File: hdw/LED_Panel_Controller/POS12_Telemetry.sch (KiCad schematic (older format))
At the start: 7 parts

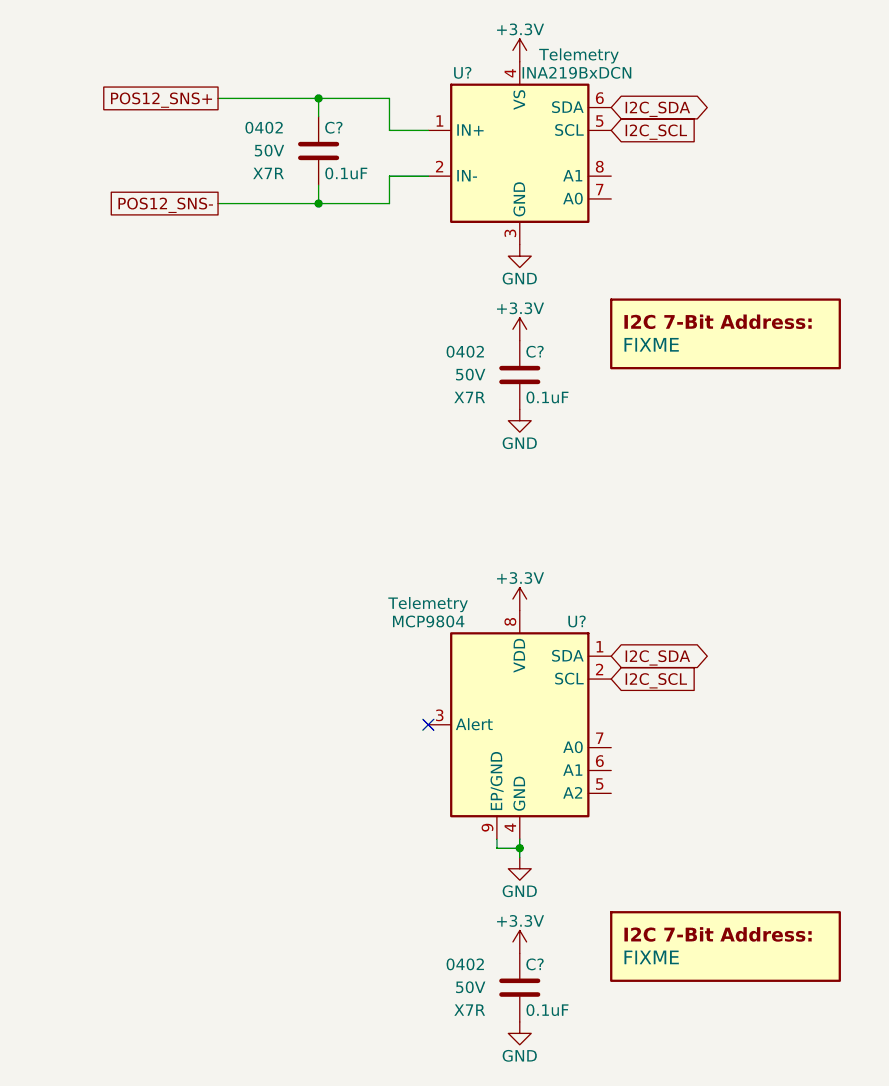
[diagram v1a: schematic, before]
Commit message: fixed level shifter sheet
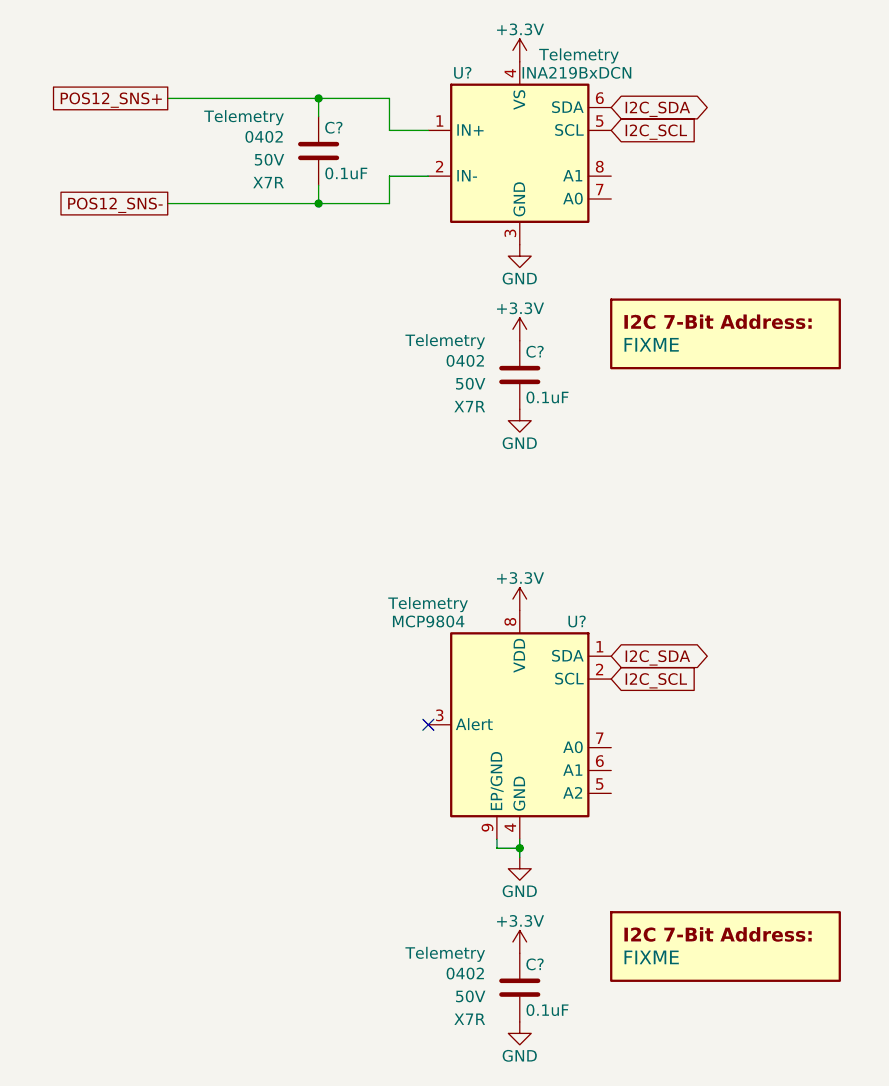
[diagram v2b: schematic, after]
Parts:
- removed C? (x3): 0.1uF, Capacitors_SMD:C_0402, symbol Custom_Library:C_Custom
- added C? (x3): 0.1uF, Capacitors_SMD:C_0402, symbol Custom_Library:C_Custom
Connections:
- net +3V3: now also C?.1, C?.1
- net GND: now also C?.2, C?.2
- net POS12_SNS+: now also C?.1
- net POS12_SNS-: now also C?.2
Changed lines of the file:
@@
 Comment4 ""
 $EndDescr
-Text GLabel 3790 1800 0    50   UnSpc ~ 0
+Text GLabel 3570 1800 0    50   UnSpc ~ 0
 POS12_SNS+
-Text GLabel 3790 2260 0    50   UnSpc ~ 0
+Text GLabel 3570 2260 0    50   UnSpc ~ 0
 POS12_SNS-
 $Comp
@@
 AR Path="/5EAE2D84/5E0ACFF2" Ref="#PWR?"  Part="1"
 AR Path="/5F581B58/5E0ACFF2" Ref="#PWR?"  Part="1"
+AR Path="/5F581B77/5E0ACFF2" Ref="#PWR?"  Part="1"
 F 0 "#PWR?" H 5110 2190 50  0001 C CNN
 F 1 "GND" H 5110 2290 50  0000 C CNN
@@
 AR Path="/5EAE2D84/5E0AD665" Ref="#PWR?"  Part="1"
 AR Path="/5F581B58/5E0AD665" Ref="#PWR?"  Part="1"
+AR Path="/5F581B77/5E0AD665" Ref="#PWR?"  Part="1"
 F 0 "#PWR?" H 5110 1490 50  0001 C CNN
 F 1 "+3.3V" H 5110 1780 50  0000 C CNN
@@
 Text GLabel 5510 1940 2    50   Input ~ 0
 I2C_SCL
-$Comp
-L Custom_Library:C_Custom C?
-U 1 1 5E0B2427
-P 5110 3010
-AR Path="/5B3E071A/5E0B2427" Ref="C?"  Part="1"
-AR Path="/5E0652BA/5E0B2427" Ref="C?"  Part="1"
-AR Path="/5E0A0E29/5E0B2427" Ref="C?"  Part="1"
-AR Path="/5E052856/5E0B2427" Ref="C?"  Part="1"
-AR Path="/5EAE2D84/5E0B2427" Ref="C?"  Part="1"
-AR Path="/5F581B58/5E0B2427" Ref="C?"  Part="1"
-F 0 "C?" H 5135 3110 50  0000 L CNN
-F 1 "0.1uF" H 5135 2910 50  0000 L CNN
-F 2 "Capacitors_SMD:C_0402" H 5148 2860 50  0001 C CNN
-F 3 "" H 5135 3110 50  0001 C CNN
-F 4 "0402" H 4960 3110 50  0000 R CNN "display_footprint"
-F 5 "50V" H 4960 3010 50  0000 R CNN "Voltage"
-F 6 "X7R" H 4960 2910 50  0000 R CNN "Dielectric"
-F 7 "" H 1200 -3870 50  0001 C CNN "Digi-Key PN"
-	1    5110 3010
-	1    0    0    -1
-$EndComp
 $Comp
 L power:+3.3V #PWR?
@@
 AR Path="/5EAE2D84/5E0B535B" Ref="#PWR?"  Part="1"
 AR Path="/5F581B58/5E0B535B" Ref="#PWR?"  Part="1"
+AR Path="/5F581B77/5E0B535B" Ref="#PWR?"  Part="1"
 F 0 "#PWR?" H 5110 2710 50  0001 C CNN
 F 1 "+3.3V" H 5110 3000 50  0000 C CNN
@@
 AR Path="/5EAE2D84/5E0B592B" Ref="#PWR?"  Part="1"
 AR Path="/5F581B58/5E0B592B" Ref="#PWR?"  Part="1"
+AR Path="/5F581B77/5E0B592B" Ref="#PWR?"  Part="1"
 F 0 "#PWR?" H 5110 2910 50  0001 C CNN
 F 1 "GND" H 5110 3010 50  0000 C CNN
@@
 AR Path="/5EAE2D84/5E0B8BC8" Ref="DOC?"  Part="1"
 AR Path="/5F581B58/5E0B8BC8" Ref="DOC?"  Part="1"
+AR Path="/5F581B77/5E0B8BC8" Ref="DOC?"  Part="1"
 F 0 "DOC?" H 6010 3130 60  0001 C CNN
 F 1 "FIXME" H 5560 2880 60  0000 L CNN
@@
 AR Path="/5EAE2D84/5E2AA995" Ref="#PWR?"  Part="1"
 AR Path="/5F581B58/5E2AA995" Ref="#PWR?"  Part="1"
+AR Path="/5F581B77/5E2AA995" Ref="#PWR?"  Part="1"
 F 0 "#PWR?" H 5110 4870 50  0001 C CNN
 F 1 "GND" H 5110 4970 50  0000 C CNN
@@
 AR Path="/5EAE2D84/5E2AA99A" Ref="#PWR?"  Part="1"
 AR Path="/5F581B58/5E2AA99A" Ref="#PWR?"  Part="1"
+AR Path="/5F581B77/5E2AA99A" Ref="#PWR?"  Part="1"
 F 0 "#PWR?" H 5110 3890 50  0001 C CNN
 F 1 "+3.3V" H 5110 4180 50  0000 C CNN
@@
 AR Path="/5EAE2D84/5E2AA99D" Ref="U?"  Part="1"
 AR Path="/5F581B58/5E2AA99D" Ref="U?"  Part="1"
+AR Path="/5F581B77/5E2AA99D" Ref="U?"  Part="1"
 F 0 "U?" H 4860 4990 50  0000 C CNN
 F 1 "MCP9804" H 5510 4990 50  0000 C CNN
@@
 NoConn ~ 4710 4540
 $Comp
-L Custom_Library:C_Custom C?
-U 1 1 5E2AA9A1
-P 5110 5690
-AR Path="/5B3E071A/5E2AA9A1" Ref="C?"  Part="1"
-AR Path="/5E0652BA/5E2AA9A1" Ref="C?"  Part="1"
-AR Path="/5E0A0E29/5E2AA9A1" Ref="C?"  Part="1"
-AR Path="/5E052856/5E2AA9A1" Ref="C?"  Part="1"
-AR Path="/5EAE2D84/5E2AA9A1" Ref="C?"  Part="1"
-AR Path="/5F581B58/5E2AA9A1" Ref="C?"  Part="1"
-F 0 "C?" H 5135 5790 50  0000 L CNN
-F 1 "0.1uF" H 5135 5590 50  0000 L CNN
-F 2 "Capacitors_SMD:C_0402" H 5148 5540 50  0001 C CNN
-F 3 "" H 5135 5790 50  0001 C CNN
-F 4 "0402" H 4960 5790 50  0000 R CNN "display_footprint"
-F 5 "50V" H 4960 5690 50  0000 R CNN "Voltage"
-F 6 "X7R" H 4960 5590 50  0000 R CNN "Dielectric"
-F 7 "" H 1200 -1190 50  0001 C CNN "Digi-Key PN"
-	1    5110 5690
-	1    0    0    -1
-$EndComp
-$Comp
 L power:+3.3V #PWR?
 U 1 1 5E2AA9A6
@@
 AR Path="/5EAE2D84/5E2AA9A6" Ref="#PWR?"  Part="1"
 AR Path="/5F581B58/5E2AA9A6" Ref="#PWR?"  Part="1"
+AR Path="/5F581B77/5E2AA9A6" Ref="#PWR?"  Part="1"
 F 0 "#PWR?" H 5110 5390 50  0001 C CNN
 F 1 "+3.3V" H 5110 5680 50  0000 C CNN
@@
 AR Path="/5EAE2D84/5E2AA9AD" Ref="#PWR?"  Part="1"
 AR Path="/5F581B58/5E2AA9AD" Ref="#PWR?"  Part="1"
+AR Path="/5F581B77/5E2AA9AD" Ref="#PWR?"  Part="1"
 F 0 "#PWR?" H 5110 5590 50  0001 C CNN
 F 1 "GND" H 5110 5690 50  0000 C CNN
@@
 AR Path="/5EAE2D84/5E2AA9AF" Ref="DOC?"  Part="1"
 AR Path="/5F581B58/5E2AA9AF" Ref="DOC?"  Part="1"
+AR Path="/5F581B77/5E2AA9AF" Ref="DOC?"  Part="1"
 F 0 "DOC?" H 6010 5810 60  0001 C CNN
 F 1 "FIXME" H 5560 5560 60  0000 L CNN
@@
 Wire Wire Line
 	4230 1880 4230 1800
-$Comp
-L Custom_Library:C_Custom C?
-U 1 1 5E07E0FD
-P 4230 2030
-AR Path="/5B3E071A/5E07E0FD" Ref="C?"  Part="1"
-AR Path="/5E0652BA/5E07E0FD" Ref="C?"  Part="1"
-AR Path="/5E0A0E29/5E07E0FD" Ref="C?"  Part="1"
-AR Path="/5E052856/5E07E0FD" Ref="C?"  Part="1"
-AR Path="/5EAE2D84/5E07E0FD" Ref="C?"  Part="1"
-AR Path="/5F581B58/5E07E0FD" Ref="C?"  Part="1"
-F 0 "C?" H 4255 2130 50  0000 L CNN
-F 1 "0.1uF" H 4255 1930 50  0000 L CNN
-F 2 "Capacitors_SMD:C_0402" H 4268 1880 50  0001 C CNN
-F 3 "" H 4255 2130 50  0001 C CNN
-F 4 "0402" H 4080 2130 50  0000 R CNN "display_footprint"
-F 5 "50V" H 4080 2030 50  0000 R CNN "Voltage"
-F 6 "X7R" H 4080 1930 50  0000 R CNN "Dielectric"
-F 7 "" H 320 -4850 50  0001 C CNN "Digi-Key PN"
-	1    4230 2030
-	1    0    0    -1
-$EndComp
-Wire Wire Line
-	3790 2260 4230 2260
-Wire Wire Line
-	3790 1800 4230 1800
 $Comp
 L Analog_ADC:INA219BxDCN U?
@@
 	4540 2260 4230 2260
 Connection ~ 4230 2260
+$Comp
+L Custom_Library:C_Custom C?
+U 1 1 6018BD18
+P 4230 2030
+AR Path="/5B3E071A/6018BD18" Ref="C?"  Part="1"
+AR Path="/5E0652BA/6018BD18" Ref="C?"  Part="1"
+AR Path="/5E0A0E29/6018BD18" Ref="C?"  Part="1"
+AR Path="/5E052856/6018BD18" Ref="C?"  Part="1"
+AR Path="/5EAE2D84/6018BD18" Ref="C?"  Part="1"
+AR Path="/5F581B58/6018BD18" Ref="C?"  Part="1"
+AR Path="/5F581B77/6018BD18" Ref="C?"  Part="1"
+F 0 "C?" H 4255 2130 50  0000 L CNN
+F 1 "0.1uF" H 4255 1930 50  0000 L CNN
+F 2 "Capacitors_SMD:C_0402" H 4268 1880 50  0001 C CNN
+F 3 "" H 4255 2130 50  0001 C CNN
+F 4 "0402" H 4080 2090 50  0000 R CNN "display_footprint"
+F 5 "50V" H 4080 1990 50  0000 R CNN "Voltage"
+F 6 "X7R" H 4080 1890 50  0000 R CNN "Dielectric"
+F 7 "Telemetry" H 4080 2180 50  0000 R CNN "Configuration"
+	1    4230 2030
+	1    0    0    -1
+$EndComp
+Wire Wire Line
+	3570 1800 4230 1800
+Wire Wire Line
+	3570 2260 4230 2260
+$Comp
+L Custom_Library:C_Custom C?
+U 1 1 6018C640
+P 5110 5690
+AR Path="/5B3E071A/6018C640" Ref="C?"  Part="1"
+AR Path="/5E0652BA/6018C640" Ref="C?"  Part="1"
+AR Path="/5E0A0E29/6018C640" Ref="C?"  Part="1"
+AR Path="/5E052856/6018C640" Ref="C?"  Part="1"
+AR Path="/5EAE2D84/6018C640" Ref="C?"  Part="1"
+AR Path="/5F581B58/6018C640" Ref="C?"  Part="1"
+AR Path="/5F581B77/6018C640" Ref="C?"  Part="1"
+F 0 "C?" H 5135 5790 50  0000 L CNN
+F 1 "0.1uF" H 5135 5590 50  0000 L CNN
+F 2 "Capacitors_SMD:C_0402" H 5148 5540 50  0001 C CNN
+F 3 "" H 5135 5790 50  0001 C CNN
+F 4 "0402" H 4960 5750 50  0000 R CNN "display_footprint"
+F 5 "50V" H 4960 5650 50  0000 R CNN "Voltage"
+F 6 "X7R" H 4960 5550 50  0000 R CNN "Dielectric"
+F 7 "Telemetry" H 4960 5840 50  0000 R CNN "Configuration"
+	1    5110 5690
+	1    0    0    -1
+$EndComp
+$Comp
+L Custom_Library:C_Custom C?
+U 1 1 6018CFFA
+P 5110 3010
+AR Path="/5B3E071A/6018CFFA" Ref="C?"  Part="1"
+AR Path="/5E0652BA/6018CFFA" Ref="C?"  Part="1"
+AR Path="/5E0A0E29/6018CFFA" Ref="C?"  Part="1"
+AR Path="/5E052856/6018CFFA" Ref="C?"  Part="1"
+AR Path="/5EAE2D84/6018CFFA" Ref="C?"  Part="1"
+AR Path="/5F581B58/6018CFFA" Ref="C?"  Part="1"
+AR Path="/5F581B77/6018CFFA" Ref="C?"  Part="1"
+F 0 "C?" H 5135 3110 50  0000 L CNN
+F 1 "0.1uF" H 5135 2910 50  0000 L CNN
+F 2 "Capacitors_SMD:C_0402" H 5148 2860 50  0001 C CNN
+F 3 "" H 5135 3110 50  0001 C CNN
+F 4 "0402" H 4960 3070 50  0000 R CNN "display_footprint"
+F 5 "50V" H 4960 2970 50  0000 R CNN "Voltage"
+F 6 "X7R" H 4960 2870 50  0000 R CNN "Dielectric"
+F 7 "Telemetry" H 4960 3160 50  0000 R CNN "Configuration"
+	1    5110 3010
+	1    0    0    -1
+$EndComp
 $EndSCHEMATC

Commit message: added digikey pns, footprints, bom scrubbed
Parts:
- C? (x3): Digi-Key PN (none) -> 490-10701-1-ND
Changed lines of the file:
@@
 F 6 "X7R" H 4080 1890 50  0000 R CNN "Dielectric"
 F 7 "Telemetry" H 4080 2180 50  0000 R CNN "Configuration"
+F 8 "490-10701-1-ND" H 4230 2030 50  0001 C CNN "Digi-Key PN"
 	1    4230 2030
 	1    0    0    -1
@@
 F 6 "X7R" H 4960 5550 50  0000 R CNN "Dielectric"
 F 7 "Telemetry" H 4960 5840 50  0000 R CNN "Configuration"
+F 8 "490-10701-1-ND" H 5110 5690 50  0001 C CNN "Digi-Key PN"
 	1    5110 5690
 	1    0    0    -1
@@
 F 6 "X7R" H 4960 2870 50  0000 R CNN "Dielectric"
 F 7 "Telemetry" H 4960 3160 50  0000 R CNN "Configuration"
+F 8 "490-10701-1-ND" H 5110 3010 50  0001 C CNN "Digi-Key PN"
 	1    5110 3010
 	1    0    0    -1

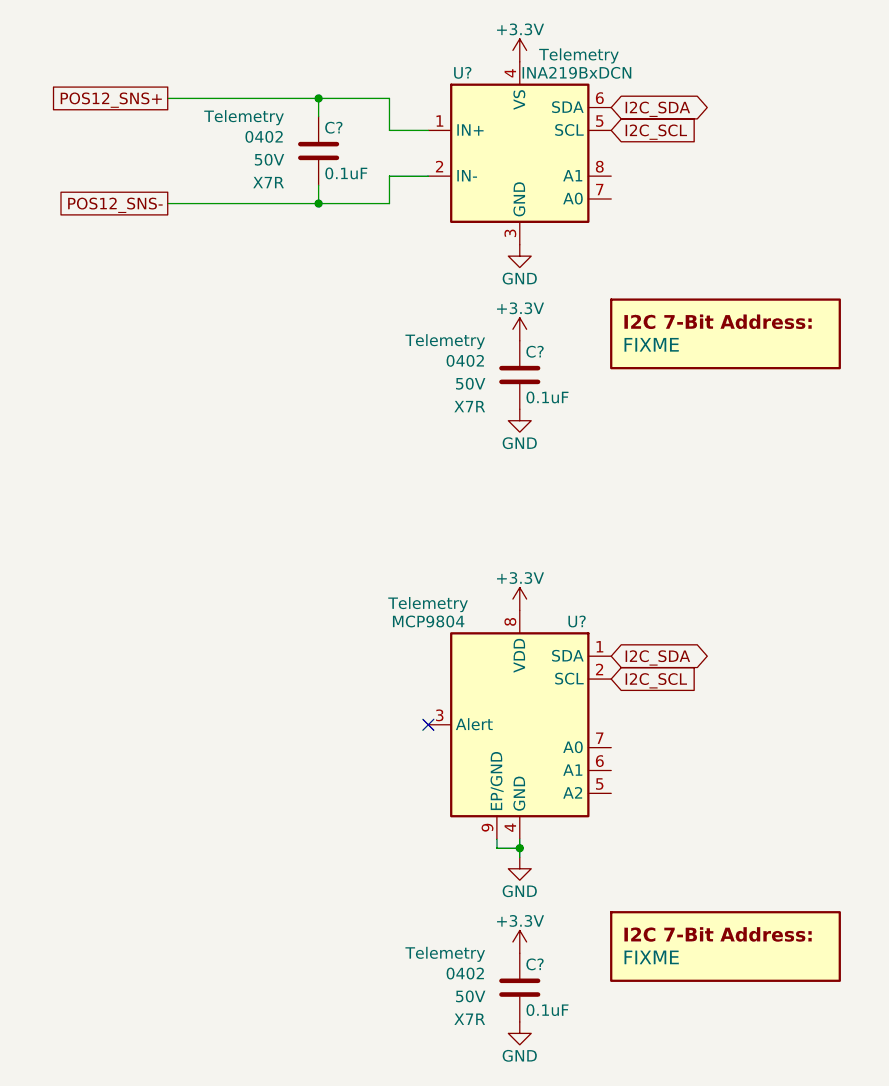
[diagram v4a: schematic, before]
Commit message: assigned I2C addresses
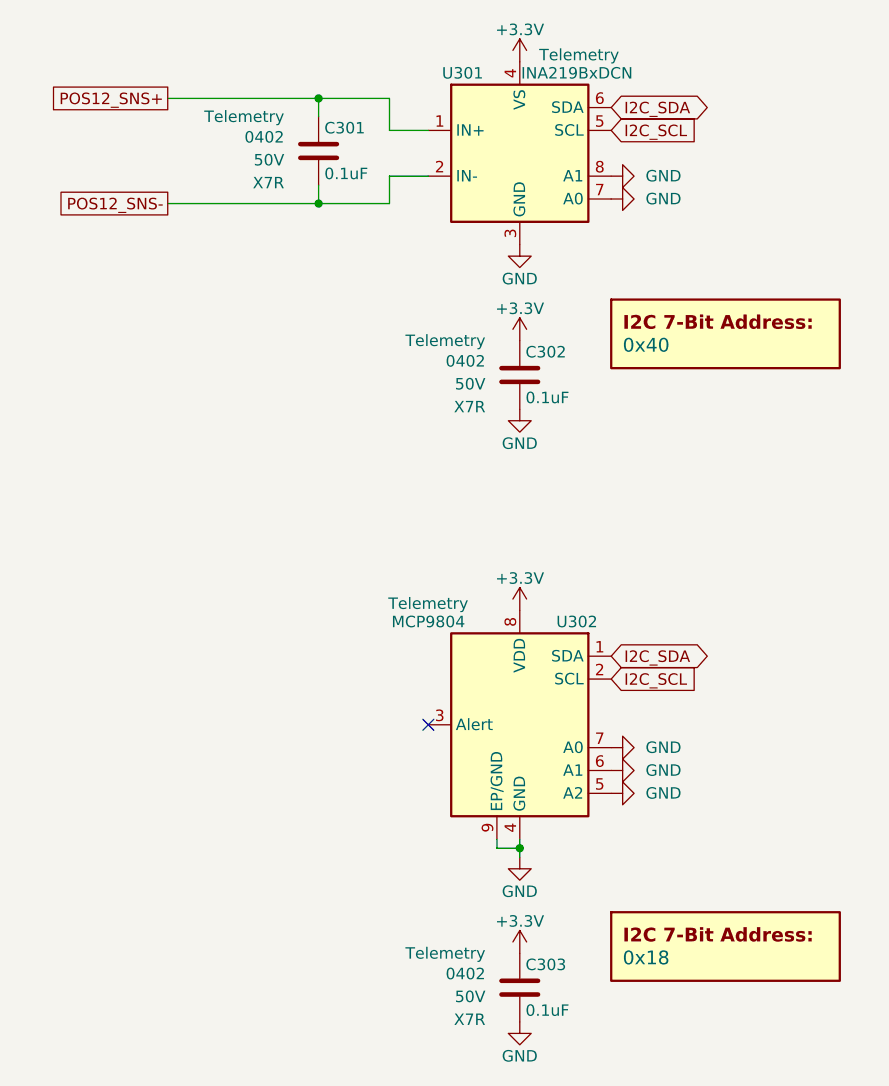
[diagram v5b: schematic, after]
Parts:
- removed C? (x3): 0.1uF, Capacitors_SMD:C_0402, symbol Custom_Library:C_Custom
- removed DOC?: FIXME, symbol Custom_Library:I2C_Address
- removed U?: MCP9804, Package_DFN_QFN:DFN-8-1EP_3x2mm_P0.5mm_EP1.3x1.5mm, symbol Sensor_Temperature:MCP9804_DFN
- added C301, C302, C303: 0.1uF, Capacitors_SMD:C_0402, symbol Custom_Library:C_Custom
- added DOC301: 0x40, symbol Custom_Library:I2C_Address
- added U302: MCP9804, Package_DFN_QFN:DFN-8-1EP_3x2mm_P0.5mm_EP1.3x1.5mm, symbol Sensor_Temperature:MCP9804_DFN
- DOC302: renamed from DOC?; value FIXME -> 0x18
- gave numbers to parts that had none: 1
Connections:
- net +3V3: now also C302.1, C303.1, U302.8 (VDD)
- net GND: now also U301.7 (A0), U301.8 (A1), C302.2, C303.2, U302.4 (GND), U302.5 (A2), U302.6 (A1), U302.7 (A0), U302.9 (EP/GND)
- net I2C_SCL: now also U302.2 (SCL)
- net I2C_SDA: now also U302.1 (SDA)
- net POS12_SNS+: now also C301.1
- net POS12_SNS-: now also C301.2

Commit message: added BOMs, some consolidation
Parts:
- C301, C302, C303: Digi-Key PN 490-10701-1-ND -> 490-10698-1-ND
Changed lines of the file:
@@
 F 6 "X7R" H 4080 1890 50  0000 R CNN "Dielectric"
 F 7 "Telemetry" H 4080 2180 50  0000 R CNN "Configuration"
-F 8 "490-10701-1-ND" H 4230 2030 50  0001 C CNN "Digi-Key PN"
+F 8 "490-10698-1-ND" H 4230 2030 50  0001 C CNN "Digi-Key PN"
 	1    4230 2030
 	1    0    0    -1
@@
 F 6 "X7R" H 4960 5550 50  0000 R CNN "Dielectric"
 F 7 "Telemetry" H 4960 5840 50  0000 R CNN "Configuration"
-F 8 "490-10701-1-ND" H 5110 5690 50  0001 C CNN "Digi-Key PN"
+F 8 "490-10698-1-ND" H 5110 5690 50  0001 C CNN "Digi-Key PN"
 	1    5110 5690
 	1    0    0    -1
@@
 F 6 "X7R" H 4960 2870 50  0000 R CNN "Dielectric"
 F 7 "Telemetry" H 4960 3160 50  0000 R CNN "Configuration"
-F 8 "490-10701-1-ND" H 5110 3010 50  0001 C CNN "Digi-Key PN"
+F 8 "490-10698-1-ND" H 5110 3010 50  0001 C CNN "Digi-Key PN"
 	1    5110 3010
 	1    0    0    -1
